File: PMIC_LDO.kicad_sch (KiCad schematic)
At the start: 1 part, among them U3 RK809

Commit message: PMIC DCDC
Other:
- company: (none) -> Qingdao IotPi Information Technology
- title: (none) -> Leaf RV1126 PMIC RK809
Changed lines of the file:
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@@
 (kicad_sch (version 20230121) (generator eeschema)
   (paper "A4")
+  (title_block
+    (title "Leaf RV1126 PMIC RK809")
+    (date "2023-02-23")
+    (rev "1")
+    (company "Qingdao IotPi Information Technology")
+  )
   (symbol (lib_id "CPU_Rockchip:RK809") (at 146.05 80.01 0) (unit 2)
     (in_bom yes) (on_board yes) (dnp no) (fields_autoplaced)

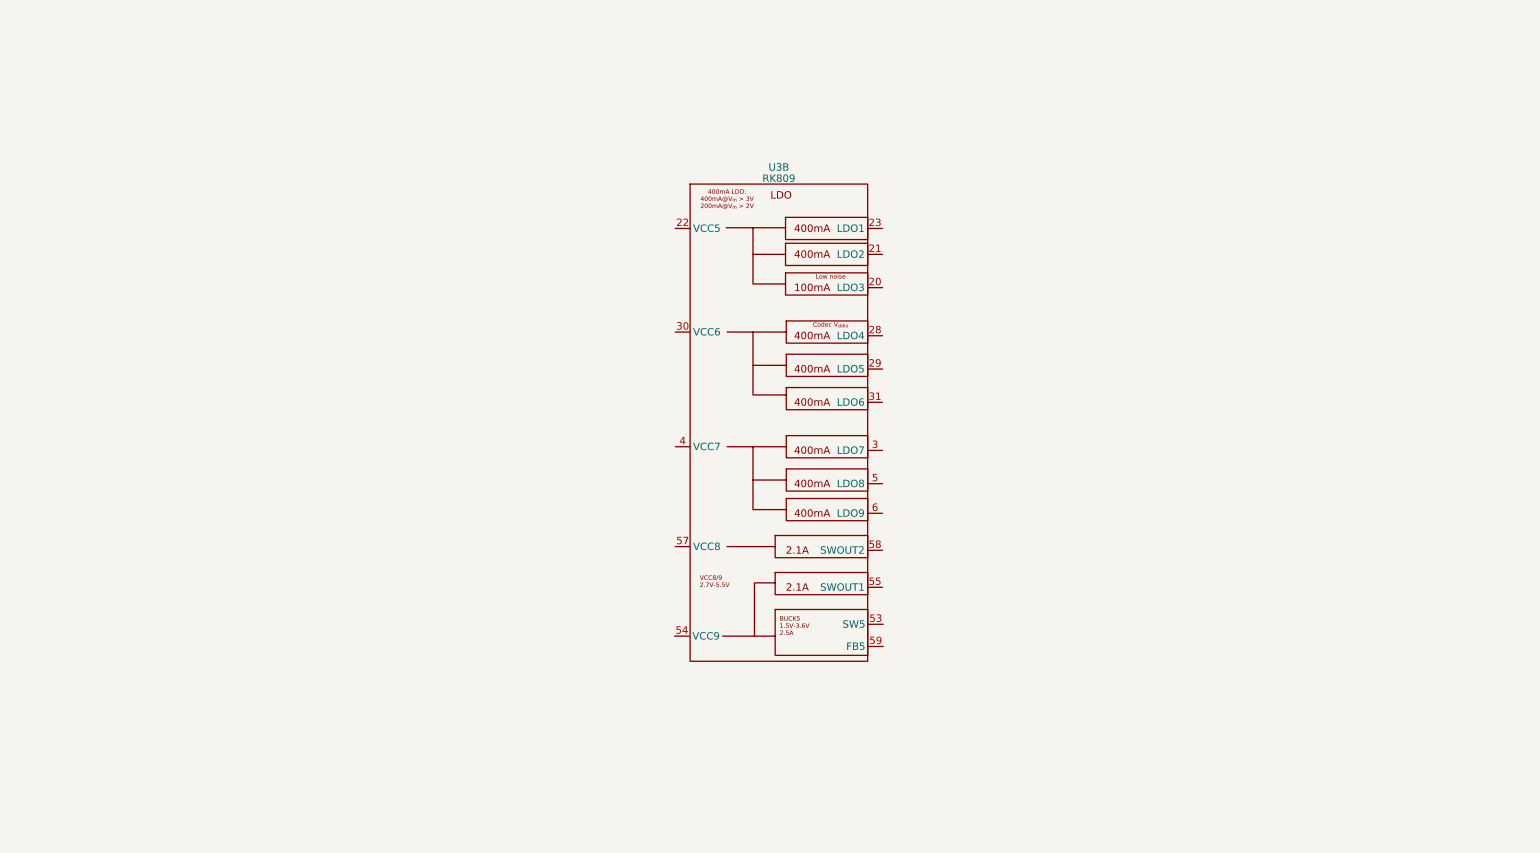
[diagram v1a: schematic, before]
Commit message: PMIC LDO
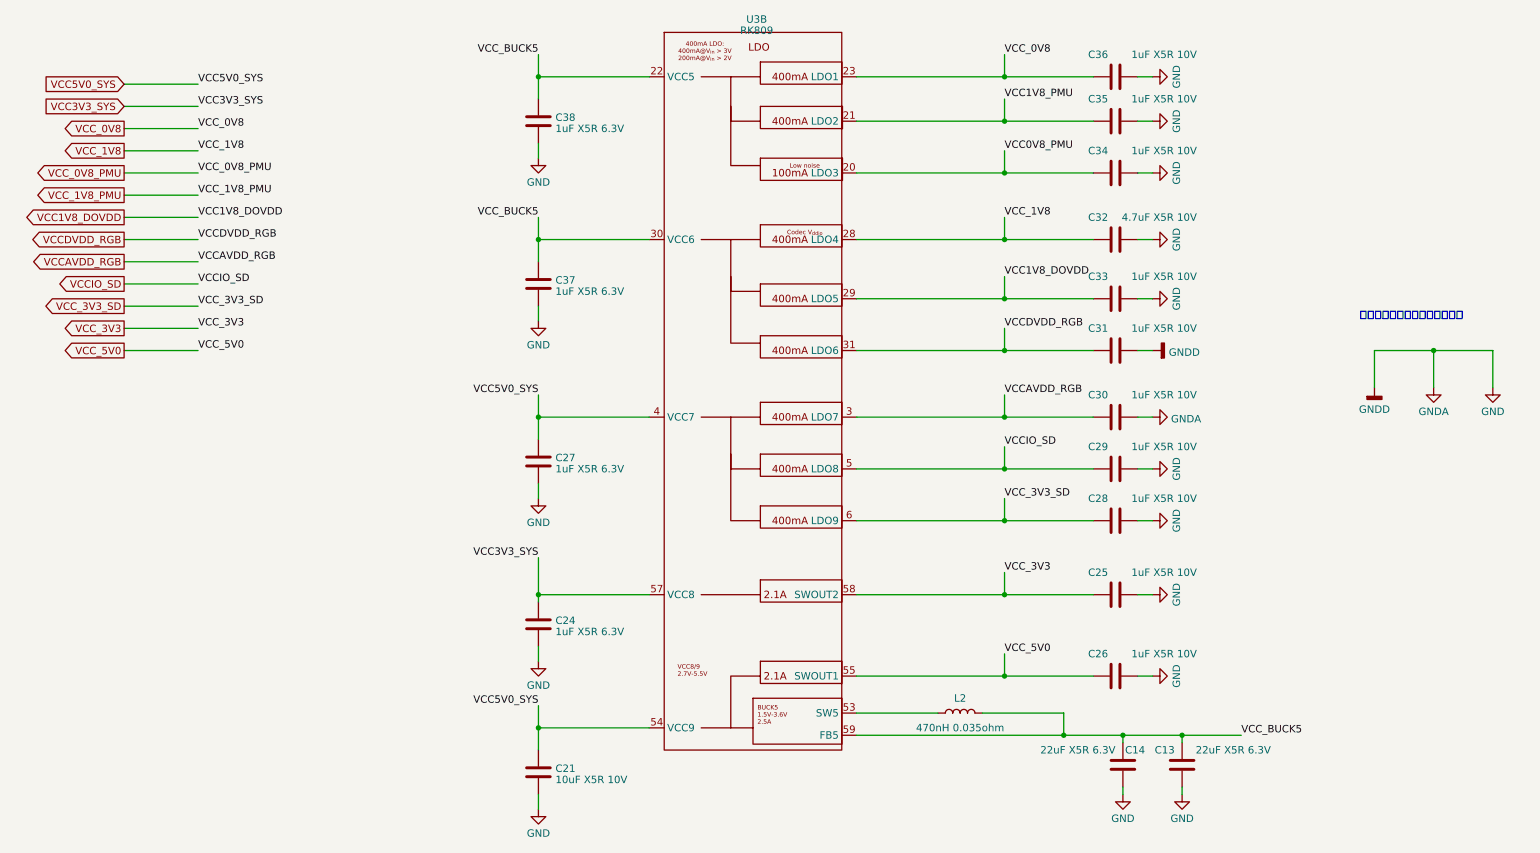
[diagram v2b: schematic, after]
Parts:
- added C13, C14: 22uF X5R 6.3V, Resistor_SMD:R_0603_1608Metric, symbol Device:C
- added C21: 10uF X5R 10V, Capacitor_SMD:C_0603_1608Metric, symbol Device:C
- added C24, C27, C37, C38: 1uF X5R 6.3V, Capacitor_SMD:C_0402_1005Metric, symbol Device:C
- added C25, C26, C28, C29, C30, C31, C33, C34, C35, C36: 1uF X5R 10V, Capacitor_SMD:C_0402_1005Metric, symbol Device:C
- added C32: 4.7uF X5R 10V, Capacitor_SMD:C_0402_1005Metric, symbol Device:C
- added L2: 470nH 0.035ohm, symbol Device:L
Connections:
- net VCC0V8_PMU: now reaches U3.20 (LDO3)
- net VCC0V8_PMU: now also C34.1
- net VCC1V8_PMU: now reaches U3.21 (LDO2)
- net VCC1V8_PMU: now also C35.1
- net VCC_BUCK5: now reaches U3.22 (VCC5)
- net VCC_BUCK5: now also U3.30 (VCC6), U3.59 (FB5), C13.1, C14.1, C37.1, C38.1, L2.1
- net VCC_0V8: now reaches U3.23 (LDO1)
- net VCC_0V8: now also C36.1
- net VCC_1V8: now reaches U3.28 (LDO4)
- net VCC_1V8: now also C32.1
- net VCC1V8_DOVDD: now reaches U3.29 (LDO5)
- net VCC1V8_DOVDD: now also C33.1
- net VCCAVDD_RGB: now reaches U3.3 (LDO7)
- net VCCAVDD_RGB: now also C30.1
- net VCCDVDD_RGB: now reaches U3.31 (LDO6)
- net VCCDVDD_RGB: now also C31.1
- net VCC5V0_SYS: now reaches U3.4 (VCC7)
- net VCC5V0_SYS: now also U3.54 (VCC9), C21.1, C27.1
- net VCCIO_SD: now reaches U3.5 (LDO8)
- net VCCIO_SD: now also C29.1
- net at U3.53 (SW5): now also L2.2
- net VCC_5V0: now reaches U3.55 (SWOUT1)
- net VCC_5V0: now also C26.1
- net VCC3V3_SYS: now reaches U3.57 (VCC8)
- net VCC3V3_SYS: now also C24.1
- net VCC_3V3: now reaches U3.58 (SWOUT2)
- net VCC_3V3: now also C25.1
- net VCC_3V3_SD: now reaches U3.6 (LDO9)
- net VCC_3V3_SD: now also C28.1
- new net GND: C13.2, C14.2, C21.2, C24.2, C25.2, C26.2, C27.2, C28.2, C29.2, C30.2, C31.2, C32.2, C33.2, C34.2, C35.2, C36.2, C37.2, C38.2
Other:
- note added: "确定数字地，模拟地的连接问题"
- moved on the sheet: U3B

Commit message: updated: PMIC codec
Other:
- title: Leaf RV1126 PMIC RK809 -> Leaf RV1126 PMIC RK809 Codec
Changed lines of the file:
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@@
   (paper "A4")
   (title_block
-    (title "Leaf RV1126 PMIC RK809")
-    (date "2023-02-23")
+    (title "Leaf RV1126 PMIC RK809 Codec")
+    (date "2023-02-25")
     (rev "1")
     (company "Qingdao IotPi Information Technology")

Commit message: updated: titles
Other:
- title: Leaf RV1126 PMIC RK809 Codec -> Leaf RV1126 RK809 LDO
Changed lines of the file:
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@@
   (paper "A4")
   (title_block
-    (title "Leaf RV1126 PMIC RK809 Codec")
+    (title "Leaf RV1126 RK809 LDO")
     (date "2023-02-25")
     (rev "1")

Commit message: changed to use GND instead of GNDD and GNDA
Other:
- note removed: "确定数字地，模拟地的连接问题"
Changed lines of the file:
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@@
   (junction (at 190.5 57.15) (diameter 0) (color 0 0 0 0)
   )
-  (junction (at 264.16 76.2) (diameter 0) (color 0 0 0 0)
-  )
   (junction (at 190.5 29.21) (diameter 0) (color 0 0 0 0)
   )
@@
     (stroke (width 0) (type default))
   )
-  (wire (pts (xy 264.16 76.2) (xy 264.16 82.55))
-    (stroke (width 0) (type default))
-  )
   (wire (pts (xy 39.37 64.77) (xy 52.07 64.77))
     (stroke (width 0) (type default))
@@
     (stroke (width 0) (type default))
   )
-  (wire (pts (xy 264.16 76.2) (xy 274.32 76.2))
-    (stroke (width 0) (type default))
-  )
   (wire (pts (xy 190.5 45.72) (xy 205.74 45.72))
     (stroke (width 0) (type default))
@@
     (stroke (width 0) (type default))
   )
-  (wire (pts (xy 254 82.55) (xy 254 76.2))
-    (stroke (width 0) (type default))
-  )
   (wire (pts (xy 213.36 45.72) (xy 215.9 45.72))
     (stroke (width 0) (type default))
@@
     (stroke (width 0) (type default))
   )
-  (wire (pts (xy 274.32 76.2) (xy 274.32 82.55))
-    (stroke (width 0) (type default))
-  )
   (wire (pts (xy 190.5 101.6) (xy 190.5 105.41))
     (stroke (width 0) (type default))
   )
-  (wire (pts (xy 254 76.2) (xy 264.16 76.2))
-    (stroke (width 0) (type default))
-  )
   (wire (pts (xy 110.49 111.76) (xy 110.49 118.11))
     (stroke (width 0) (type default))
@@
   (wire (pts (xy 110.49 118.11) (xy 110.49 119.38))
     (stroke (width 0) (type default))
-  )
-  (text "确定数字地，模拟地的连接问题" (at 251.46 71.12 0)
-    (effects (font (size 1.27 1.27)) (justify left bottom))
   )
   (label "VCC5V0_SYS" (at 52.07 30.48 0) (fields_autoplaced)
@@
     )
   )
-  (symbol (lib_id "power:GNDA") (at 264.16 82.55 0) (unit 1)
-    (in_bom yes) (on_board yes) (dnp no) (fields_autoplaced)
-    (property "Reference" "#PWR039" (at 264.16 88.9 0)
-      (effects (font (size 1.27 1.27)) hide)
-    )
-    (property "Value" "GNDA" (at 264.16 86.6855 0)
-      (effects (font (size 1.27 1.27)))
-    )
-    (property "Footprint" "" (at 264.16 82.55 0)
-      (effects (font (size 1.27 1.27)) hide)
-    )
-    (property "Datasheet" "" (at 264.16 82.55 0)
-      (effects (font (size 1.27 1.27)) hide)
-    )
-    (pin "1")
-    (instances
-      (project "leaf"
-        (path "/e3b58043-16a3-43c8-9fad-9c9784eebfa4/cc9fb3ac-19c3-47a8-ba7d-678b4d514ff0/46e9a7bf-8506-4399-90d8-57d007223126/587d28a9-c2cd-4fab-a2bd-304064dd6f5e"
-          (reference "#PWR039") (unit 1)
-        )
-      )
-    )
-  )
   (symbol (lib_id "Device:C") (at 110.49 123.19 0) (unit 1)
     (in_bom yes) (on_board yes) (dnp no) (fields_autoplaced)
@@
         (path "/e3b58043-16a3-43c8-9fad-9c9784eebfa4/cc9fb3ac-19c3-47a8-ba7d-678b4d514ff0/46e9a7bf-8506-4399-90d8-57d007223126/587d28a9-c2cd-4fab-a2bd-304064dd6f5e"
           (reference "C24") (unit 1)
+        )
+      )
+    )
+  )
+  (symbol (lib_id "power:GND") (at 215.9 76.2 90) (unit 1)
+    (in_bom yes) (on_board yes) (dnp no) (fields_autoplaced)
+    (property "Reference" "#PWR048" (at 222.25 76.2 0)
+      (effects (font (size 1.27 1.27)) hide)
+    )
+    (property "Value" "GND" (at 220.0355 76.2 0)
+      (effects (font (size 1.27 1.27)))
+    )
+    (property "Footprint" "" (at 215.9 76.2 0)
+      (effects (font (size 1.27 1.27)) hide)
+    )
+    (property "Datasheet" "" (at 215.9 76.2 0)
+      (effects (font (size 1.27 1.27)) hide)
+    )
+    (pin "1")
+    (instances
+      (project "leaf"
+        (path "/e3b58043-16a3-43c8-9fad-9c9784eebfa4/cc9fb3ac-19c3-47a8-ba7d-678b4d514ff0/46e9a7bf-8506-4399-90d8-57d007223126/587d28a9-c2cd-4fab-a2bd-304064dd6f5e"
+          (reference "#PWR048") (unit 1)
         )
       )
@@
     )
   )
-  (symbol (lib_id "power:GNDA") (at 215.9 87.63 90) (unit 1)
+  (symbol (lib_id "power:GND") (at 215.9 87.63 90) (unit 1)
     (in_bom yes) (on_board yes) (dnp no) (fields_autoplaced)
     (property "Reference" "#PWR047" (at 222.25 87.63 0)
       (effects (font (size 1.27 1.27)) hide)
     )
-    (property "Value" "GNDA" (at 219.075 87.9468 90)
-      (effects (font (size 1.27 1.27)) (justify right))
+    (property "Value" "GND" (at 220.0355 87.63 0)
+      (effects (font (size 1.27 1.27)))
     )
     (property "Footprint" "" (at 215.9 87.63 0)
@@
         (path "/e3b58043-16a3-43c8-9fad-9c9784eebfa4/cc9fb3ac-19c3-47a8-ba7d-678b4d514ff0/46e9a7bf-8506-4399-90d8-57d007223126/587d28a9-c2cd-4fab-a2bd-304064dd6f5e"
           (reference "#PWR029") (unit 1)
-        )
-      )
-    )
-  )
-  (symbol (lib_id "power:GND") (at 274.32 82.55 0) (unit 1)
-    (in_bom yes) (on_board yes) (dnp no) (fields_autoplaced)
-    (property "Reference" "#PWR049" (at 274.32 88.9 0)
-      (effects (font (size 1.27 1.27)) hide)
-    )
-    (property "Value" "GND" (at 274.32 86.6855 0)
-      (effects (font (size 1.27 1.27)))
-    )
-    (property "Footprint" "" (at 274.32 82.55 0)
-      (effects (font (size 1.27 1.27)) hide)
-    )
-    (property "Datasheet" "" (at 274.32 82.55 0)
-      (effects (font (size 1.27 1.27)) hide)
-    )
-    (pin "1")
-    (instances
-      (project "leaf"
-        (path "/e3b58043-16a3-43c8-9fad-9c9784eebfa4/cc9fb3ac-19c3-47a8-ba7d-678b4d514ff0/46e9a7bf-8506-4399-90d8-57d007223126/587d28a9-c2cd-4fab-a2bd-304064dd6f5e"
-          (reference "#PWR049") (unit 1)
         )
       )
@@
     )
   )
-  (symbol (lib_id "power:GNDD") (at 215.9 76.2 90) (unit 1)
-    (in_bom yes) (on_board yes) (dnp no) (fields_autoplaced)
-    (property "Reference" "#PWR048" (at 222.25 76.2 0)
-      (effects (font (size 1.27 1.27)) hide)
-    )
-    (property "Value" "GNDD" (at 218.694 76.5168 90)
-      (effects (font (size 1.27 1.27)) (justify right))
-    )
-    (property "Footprint" "" (at 215.9 76.2 0)
-      (effects (font (size 1.27 1.27)) hide)
-    )
-    (property "Datasheet" "" (at 215.9 76.2 0)
-      (effects (font (size 1.27 1.27)) hide)
-    )
-    (pin "1")
-    (instances
-      (project "leaf"
-        (path "/e3b58043-16a3-43c8-9fad-9c9784eebfa4/cc9fb3ac-19c3-47a8-ba7d-678b4d514ff0/46e9a7bf-8506-4399-90d8-57d007223126/587d28a9-c2cd-4fab-a2bd-304064dd6f5e"
-          (reference "#PWR048") (unit 1)
-        )
-      )
-    )
-  )
   (symbol (lib_id "Device:C") (at 209.55 67.31 90) (unit 1)
     (in_bom yes) (on_board yes) (dnp no)
@@
         )
       )
-    )
-  )
-  (symbol (lib_id "power:GNDD") (at 254 82.55 0) (unit 1)
-    (in_bom yes) (on_board yes) (dnp no) (fields_autoplaced)
-    (property "Reference" "#PWR038" (at 254 88.9 0)
-      (effects (font (size 1.27 1.27)) hide)
-    )
-    (property "Value" "GNDD" (at 254 86.3045 0)
-      (effects (font (size 1.27 1.27)))
-    )
-    (property "Footprint" "" (at 254 82.55 0)
-      (effects (font (size 1.27 1.27)) hide)
-    )
-    (property "Datasheet" "" (at 254 82.55 0)
-      (effects (font (size 1.27 1.27)) hide)
-    )
-    (pin "1")
-    (instances
-      (project "leaf"
-        (path "/e3b58043-16a3-43c8-9fad-9c9784eebfa4/cc9fb3ac-19c3-47a8-ba7d-678b4d514ff0/46e9a7bf-8506-4399-90d8-57d007223126/587d28a9-c2cd-4fab-a2bd-304064dd6f5e"
-          (reference "#PWR038") (unit 1)
-        )
-      )

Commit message: Updated eMMC
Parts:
- U3: value RK809 -> RK809-2
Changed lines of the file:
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@@
       (effects (font (size 1.27 1.27)))
     )
-    (property "Value" "RK809" (at 147.955 21.2631 0)
+    (property "Value" "RK809-2" (at 147.955 21.2631 0)
       (effects (font (size 1.27 1.27)))
     )

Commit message: updated footprints
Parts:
- renumbered C38 to C62, C37 to C63, C27 to C64, C24 to C65, C21 to C66, C36 to C67, C35 to C68, C34 to C69, C32 to C70, C33 to C71, C31 to C72, C30 to C73, C29 to C74, C28 to C75, C25 to C76, C26 to C77, U3 to U5

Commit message: updated Capacitors
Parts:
- C62, C63, C64, C65: footprint Capacitor_SMD:C_0402_1005Metric -> Capacitor_SMD:C_0201_0603Metric; LCSC (none) -> C76929; Model (none) -> GRM033R60J105KEA2D; Vendor (none) -> muRata(村田)
- C66: LCSC (none) -> C469532; Model (none) -> GRM188B31A106KE69D; Vendor (none) -> muRata(村田)
- C70: LCSC (none) -> C77004; Model (none) -> GRM155R61A475KEAAD; Vendor (none) -> muRata(村田)
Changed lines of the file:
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@@
       (effects (font (size 1.27 1.27)) (justify left))
     )
-    (property "Footprint" "Capacitor_SMD:C_0402_1005Metric" (at 111.4552 127 0)
+    (property "Footprint" "Capacitor_SMD:C_0201_0603Metric" (at 111.4552 127 0)
       (effects (font (size 1.27 1.27)) hide)
     )
     (property "Datasheet" "~" (at 110.49 123.19 0)
+      (effects (font (size 1.27 1.27)) hide)
+    )
+    (property "Description" "容值: 1uF 精度: ±10% 额定电压: 6.3V 材质(温度系数): X5R 材质:X5R" (at 110.49 123.19 0)
+      (effects (font (size 1.27 1.27)) hide)
+    )
+    (property "LCSC" "C76929" (at 110.49 123.19 0)
+      (effects (font (size 1.27 1.27)) hide)
+    )
+    (property "Model" "GRM033R60J105KEA2D" (at 110.49 123.19 0)
+      (effects (font (size 1.27 1.27)) hide)
+    )
+    (property "Vendor" "muRata(村田)" (at 110.49 123.19 0)
       (effects (font (size 1.27 1.27)) hide)
     )
@@
       (effects (font (size 1.27 1.27)) (justify left))
     )
-    (property "Footprint" "Capacitor_SMD:C_0402_1005Metric" (at 111.4552 40.64 0)
+    (property "Footprint" "Capacitor_SMD:C_0201_0603Metric" (at 111.4552 40.64 0)
       (effects (font (size 1.27 1.27)) hide)
     )
     (property "Datasheet" "~" (at 110.49 36.83 0)
+      (effects (font (size 1.27 1.27)) hide)
+    )
+    (property "Description" "容值: 1uF 精度: ±10% 额定电压: 6.3V 材质(温度系数): X5R 材质:X5R" (at 110.49 36.83 0)
+      (effects (font (size 1.27 1.27)) hide)
+    )
+    (property "LCSC" "C76929" (at 110.49 36.83 0)
+      (effects (font (size 1.27 1.27)) hide)
+    )
+    (property "Model" "GRM033R60J105KEA2D" (at 110.49 36.83 0)
+      (effects (font (size 1.27 1.27)) hide)
+    )
+    (property "Vendor" "muRata(村田)" (at 110.49 36.83 0)
       (effects (font (size 1.27 1.27)) hide)
     )
@@
       (effects (font (size 1.27 1.27)) (justify left))
     )
-    (property "Footprint" "Capacitor_SMD:C_0402_1005Metric" (at 111.4552 68.58 0)
+    (property "Footprint" "Capacitor_SMD:C_0201_0603Metric" (at 111.4552 68.58 0)
       (effects (font (size 1.27 1.27)) hide)
     )
     (property "Datasheet" "~" (at 110.49 64.77 0)
+      (effects (font (size 1.27 1.27)) hide)
+    )
+    (property "Description" "容值: 1uF 精度: ±10% 额定电压: 6.3V 材质(温度系数): X5R 材质:X5R" (at 110.49 64.77 0)
+      (effects (font (size 1.27 1.27)) hide)
+    )
+    (property "LCSC" "C76929" (at 110.49 64.77 0)
+      (effects (font (size 1.27 1.27)) hide)
+    )
+    (property "Model" "GRM033R60J105KEA2D" (at 110.49 64.77 0)
+      (effects (font (size 1.27 1.27)) hide)
+    )
+    (property "Vendor" "muRata(村田)" (at 110.49 64.77 0)
       (effects (font (size 1.27 1.27)) hide)
     )
@@
       (effects (font (size 1.27 1.27)) (justify left))
     )
-    (property "Footprint" "Capacitor_SMD:C_0402_1005Metric" (at 111.4552 99.06 0)
+    (property "Footprint" "Capacitor_SMD:C_0201_0603Metric" (at 111.4552 99.06 0)
       (effects (font (size 1.27 1.27)) hide)
     )
     (property "Datasheet" "~" (at 110.49 95.25 0)
+      (effects (font (size 1.27 1.27)) hide)
+    )
+    (property "Description" "容值: 1uF 精度: ±10% 额定电压: 6.3V 材质(温度系数): X5R 材质:X5R" (at 110.49 95.25 0)
+      (effects (font (size 1.27 1.27)) hide)
+    )
+    (property "LCSC" "C76929" (at 110.49 95.25 0)
+      (effects (font (size 1.27 1.27)) hide)
+    )
+    (property "Model" "GRM033R60J105KEA2D" (at 110.49 95.25 0)
+      (effects (font (size 1.27 1.27)) hide)
+    )
+    (property "Vendor" "muRata(村田)" (at 110.49 95.25 0)
       (effects (font (size 1.27 1.27)) hide)
     )
@@
       (effects (font (size 1.27 1.27)) hide)
     )
+    (property "Description" "容值: 10uF 精度: ±10% 额定电压: 10V 材质(温度系数): B B(JIS)" (at 110.49 148.59 0)
+      (effects (font (size 1.27 1.27)) hide)
+    )
+    (property "LCSC" "C469532" (at 110.49 148.59 0)
+      (effects (font (size 1.27 1.27)) hide)
+    )
+    (property "Model" "GRM188B31A106KE69D" (at 110.49 148.59 0)
+      (effects (font (size 1.27 1.27)) hide)
+    )
+    (property "Vendor" "muRata(村田)" (at 110.49 148.59 0)
+      (effects (font (size 1.27 1.27)) hide)
+    )
     (pin "1")
     (pin "2")
@@
       (effects (font (size 1.27 1.27)) hide)
     )
+    (property "Description" "容值: 4.7uF 精度: ±10% 额定电压: 10V 材质(温度系数): X5R 材质:X5R" (at 209.55 57.15 0)
+      (effects (font (size 1.27 1.27)) hide)
+    )
+    (property "LCSC" "C77004" (at 209.55 57.15 0)
+      (effects (font (size 1.27 1.27)) hide)
+    )
+    (property "Model" "GRM155R61A475KEAAD" (at 209.55 57.15 0)
+      (effects (font (size 1.27 1.27)) hide)
+    )
+    (property "Vendor" "muRata(村田) " (at 209.55 57.15 0)
+      (effects (font (size 1.27 1.27)) hide)
+    )
